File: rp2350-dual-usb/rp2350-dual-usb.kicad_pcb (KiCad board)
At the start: 4 copper layers, 51 x 32 mm, 60 parts, among them J1 Conn_01x03_MountingPin, J2 USB_C_Receptacle_USB2.0_16P, J3 USB_C_Receptacle_USB2.0_14P, J4 TRS, J5 TRS, SW1 Button_Switch_SMD_Push_1P1T_W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, U1 LDL1117-3.3, U2 RP2354_60QFN, U3 USBLC6-2SC6, U4 USBLC6-2SC6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

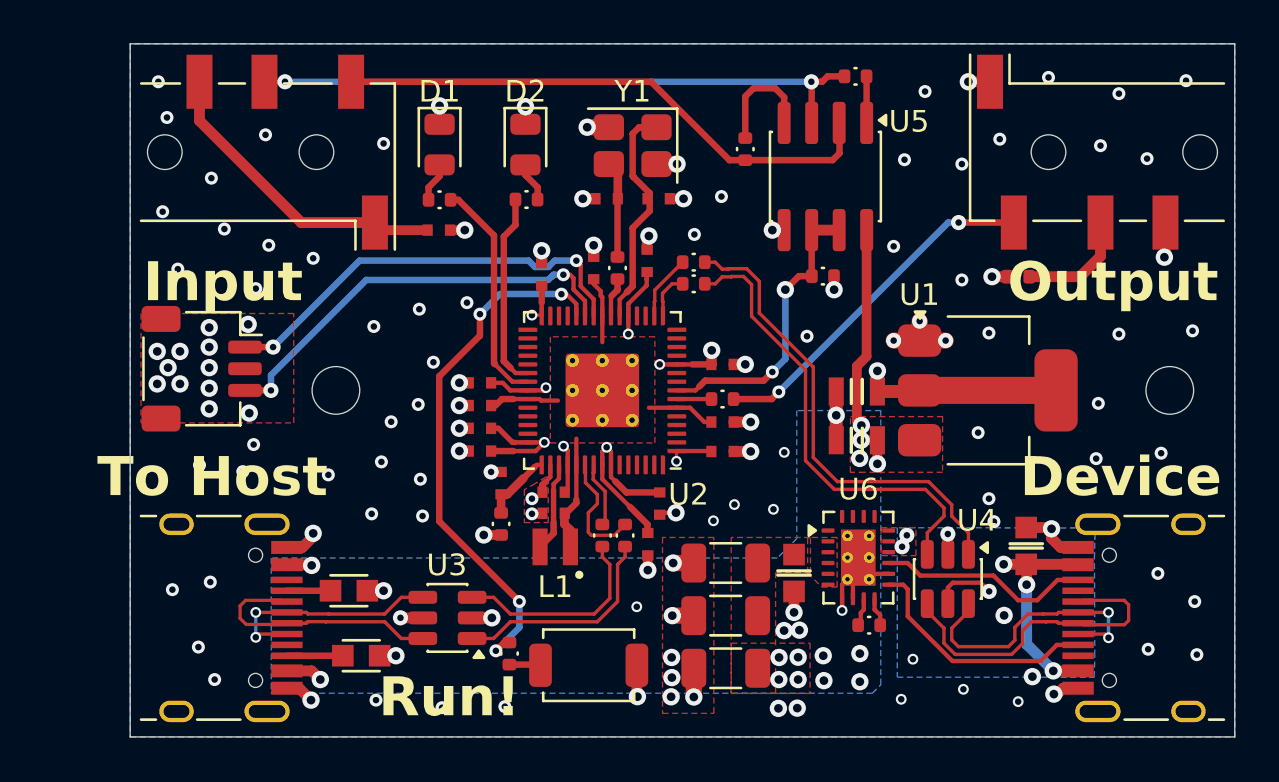
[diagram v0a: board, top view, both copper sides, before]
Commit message: feat: Updates Crustose, Cladonia and YouMe Transformer. Adds Stereo Latencies.
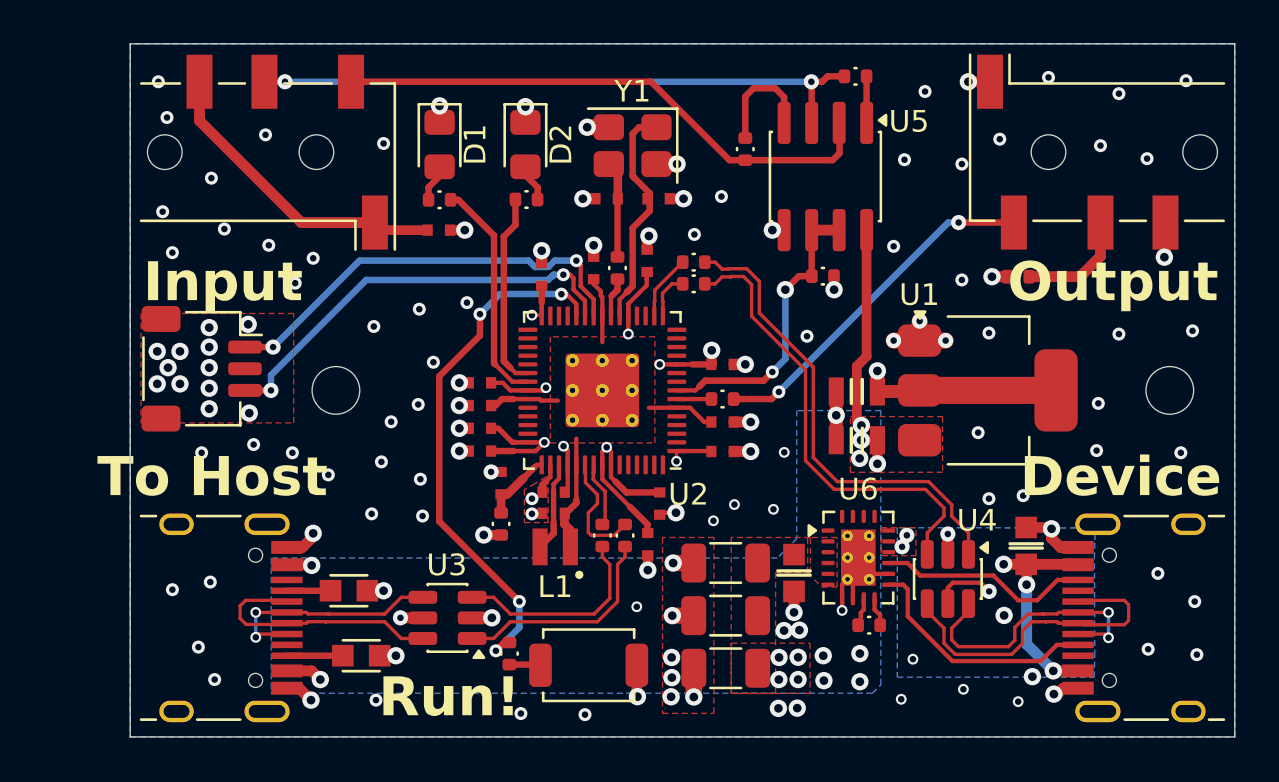
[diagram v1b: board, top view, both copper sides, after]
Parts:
- C20: value 100nF_0402_16V -> 100nF
- D1, D2: footprint LED_SMD:LED_0805_2012Metric -> LED_SMD:LED_0805_2012Metric_Pad1.15x1.40mm_HandSolder
- R1: value 33R_0402 -> 33R
- SW1: value Button_Switch_SMD_Push_1P1T_Wurth -> 1P1T Switch
